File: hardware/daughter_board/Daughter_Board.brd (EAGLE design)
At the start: 65 x 30 mm, 75 parts, among them IC1 LMV358MMX, IC2 LMV358MMX, IC3 ATMEGA2560-16AU, IC4 ATMEGA16U2-MU, IC5 LMV358MMX, IC6 LP2985-33DBVR, IC7 LMV358IDGKR, IC8 LMV358MMX, IC9 LMV358MMX, J1 USB_MINI-B_SMT, T1 FDN340P, Y1 CSTCE16M0V53-R0 16MHZ, Y2 16MHz

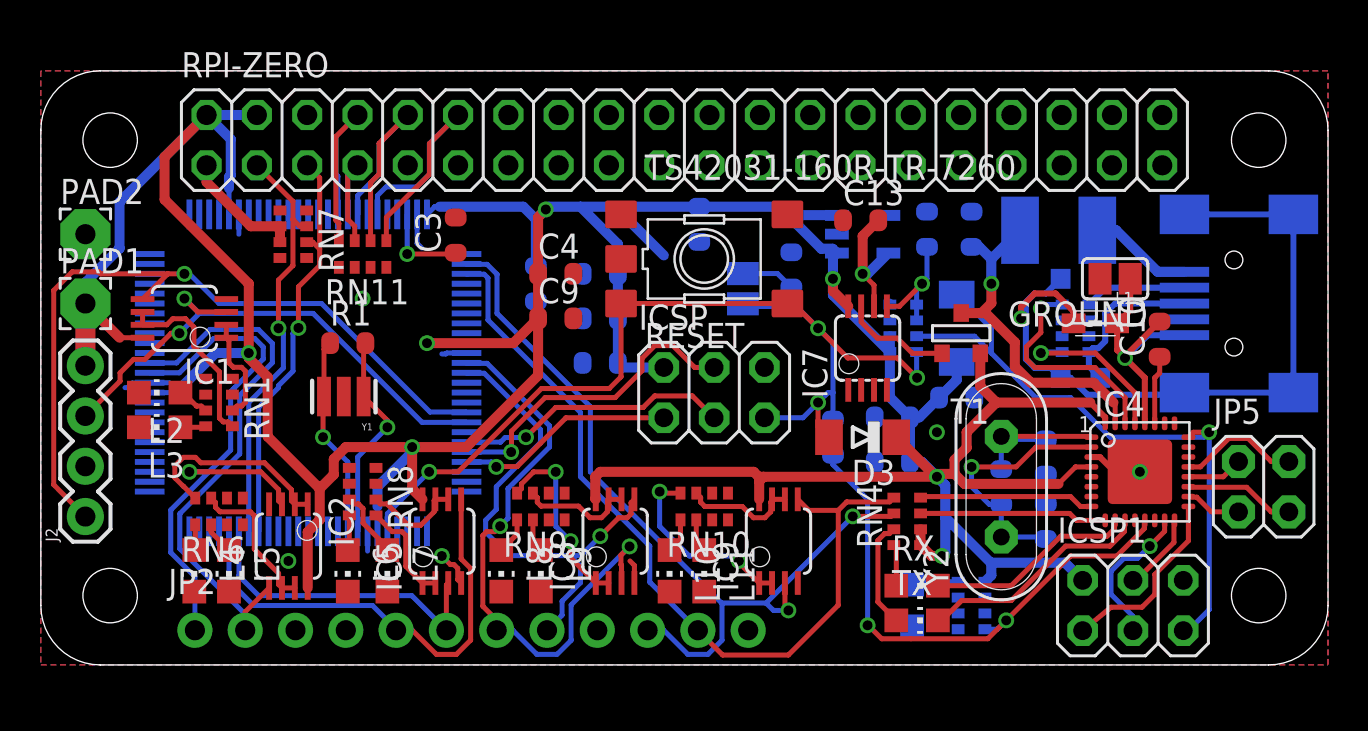
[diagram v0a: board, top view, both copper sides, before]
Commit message: partial implementation of daughter board with rpi as bootloader
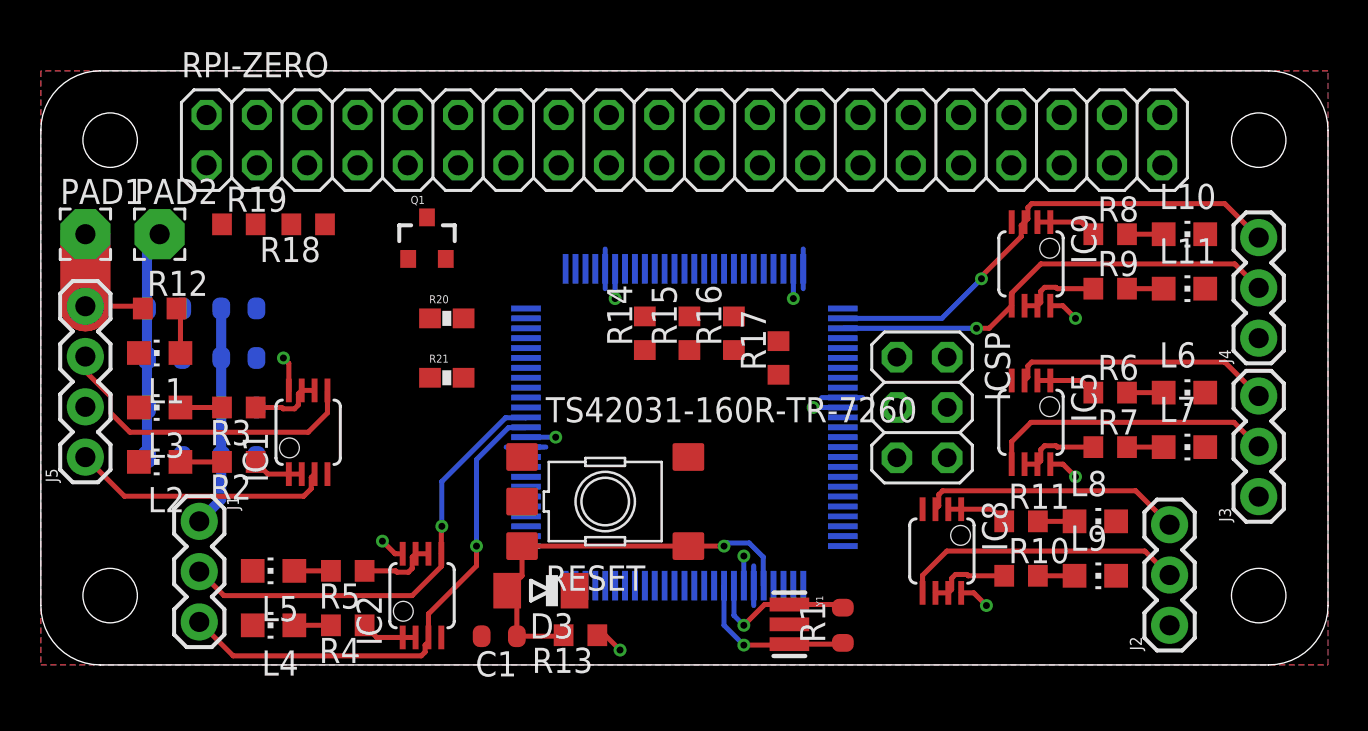
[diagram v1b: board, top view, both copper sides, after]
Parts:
- removed C10, C13: 1u, SmartPrj:C0603-ROUND
- removed C11, C12, C6, C7, C8, C9: 100n, SmartPrj:C0603-ROUND
- removed C14, C15: 22p, SmartPrj:C0603-ROUND
- removed D2: CD1206-S01575, diode:MINIMELF
- removed F1: MF-MSMF050-2 500mA, rcl:L1812
- removed GROUND, RESET-EN: (no value), jumper:SJ
- removed IC4: ATMEGA16U2-MU, SmartPrj:MLF32
- removed IC6: LP2985-33DBVR, SmartPrj:SOT23-DBV
- removed IC7: LMV358IDGKR, linear:MSOP08
- removed ICSP1: 3x2M, SmartPrj:2X03
- removed JP2: (no value), adafruit:1X12-CB
- removed JP5: 2x2M - NM, SmartPrj:2X02
- removed ON: GREEN, led:CHIP-LED0805
- removed RN1, RN10, RN11, RN3, RN4, RN6, RN8, RN9: 1k, resistor-dil:CAY16
- removed RN2: 22R, resistor-dil:CAY16
- removed RN5, RN7: 10K, resistor-dil:CAT16
- removed RX, TX: YELLOW, led:CHIP-LED0805
- removed T1: FDN340P, zetex:SOT-23
- removed Y2: 16MHz, SmartPrj:QS
- removed Z1, Z2: CG0603MLC-05E, varistor:CT/CN0603
- added J3, J4: (no value), SparkFun-Connectors:1X03
- added J5: (no value), SparkFun-Connectors:1X04
- added Q1: BSS138, SparkFun:SOT23-3
- added R10, R11, R12, R3, R4, R5, R6, R7, R8, R9: 1k, resistor:R0603
- added R13, R14, R15, R16, R17, R18, R19: 10k, resistor:R0603
- added R20, R21: 10K, SparkFun:0603-RES
- J1: value USB_MINI-B_SMT -> (none); device SparkFun-Connectors:USB-MINIB -> SparkFun-Connectors:1X03
- J2: device SparkFun-Connectors:1X04 -> SparkFun-Connectors:1X03
- L1: value BLM21 -> GREEN; device wuerth-elektronik:0805 -> led:CHIP-LED0805
- R2: value 1M -> 1k; device SmartPrj:R0603-ROUND -> resistor:R0603
- moved J2 55.0 mm to (57.0, 2.00)
- moved J1 53.4 mm to (8.00, 7.25), flipped to the top, turned to 270 degrees
- moved L1 47.3 mm to (6.00, 15.8), turned to 90 degrees
- moved L6 43.2 mm to (57.8, 13.8), turned to 270 degrees
- moved L7 40.7 mm to (57.8, 11.0), turned to 270 degrees
- moved R2 38.5 mm to (10.0, 10.2), flipped to the top, turned to 180 degrees
- moved C5 36.9 mm to (6.25, 15.5)
- moved L10 31.1 mm to (57.8, 21.8), turned to 270 degrees
- moved IC5 30.3 mm to (50.0, 12.2), turned to 180 degrees
- moved L8 30.1 mm to (53.2, 7.25), turned to 270 degrees
- moved R1 28.8 mm to (40.5, 2.00), turned to 90 degrees
- moved L11 28.1 mm to (57.8, 19.0), turned to 270 degrees
- moved L9 28.0 mm to (53.2, 4.50), turned to 270 degrees
- moved C2 26.1 mm to (10.0, 10.5), turned to 180 degrees
- moved Y1 25.3 mm to (37.8, 2.05), turned to 270 degrees
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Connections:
- removed net +3V3: C13.2, IC6.5, IC7.6
- removed net 3V3_OUT_2: RPI-ZERO.17
- removed net 8PB4: IC4.18, JP5.1
- removed net 8PB5: IC4.19, JP5.3
- removed net 8PB6: IC4.20, JP5.2
- removed net 8PB7: IC4.21, JP5.4
- removed net AREF: C3.1, IC3.98
- removed net CMP: C12.2, IC7.5, RN5.5, RN5.6
- removed net D+: J1.D+, RN2.8, Z2.2
- removed net D-: J1.D-, RN2.5, Z1.2
- removed net DTR: C7.1, IC4.13, RN3.4
- removed net GATE_CMD: IC7.7, T1.3
- removed net M8RXD: IC4.9, RN4.7
- removed net M8TXD: IC4.8, RN4.8
- removed net MISO2: IC4.17, ICSP1.1
- removed net MOSI2: IC4.16, ICSP1.4
- removed net N$54: RN4.4, RX.A
- removed net N$55: RN4.3, TX.A
- removed net PA0: IC3.78
- removed net PA1: IC3.77
- removed net PA2: IC3.76
- removed net PA3: IC3.75
- removed net PA4: IC3.74
- removed net PA5: IC3.73
- removed net PA6: IC3.72
- removed net PA7: IC3.71
- removed net PB0: IC3.19
- removed net PB4: IC3.23
- removed net PB5: IC3.24
- removed net PB6: IC3.25
- removed net PB7: IC3.26
- removed net PC0: IC3.53
- removed net PC1: IC3.54
- removed net PC2: IC3.55
- removed net PC3: IC3.56
- removed net PC4: IC3.57
- removed net PC5: IC3.58
- removed net PC6: IC3.59
- removed net PC7: IC3.60
- removed net PD7: IC3.50
- removed net PF0: IC3.97
- removed net PF1: IC3.96
- removed net PF3: IC3.94
- removed net PF7: IC3.90
- removed net PG0: IC3.51
- removed net PG1: IC3.52
- removed net PG2: IC3.70
- removed net PH3: IC3.15
- removed net PH4: IC3.16
- removed net PL0: IC3.35
- removed net PL1: IC3.36
- removed net PL2: IC3.37
- removed net PL3: IC3.38
- removed net PL4: IC3.39
- removed net PL5: IC3.40
- removed net PL6: IC3.41
- removed net PL7: IC3.42
- removed net RD+: IC4.29, RN2.1
- removed net RD-: IC4.30, RN2.4
- removed net RESET2: D2.A, IC4.24, ICSP1.5, RN5.7
- removed net RXL: IC4.10, RX.C
- removed net SCK2: IC4.15, ICSP1.3
- removed net TXL: IC4.11, TX.C
- removed net UGND: C10.2, GROUND.1, IC4.28, J1.GND, L1.1
- removed net USBVCC: C8.1, F1.1, IC4.31, T1.1
- removed net USHIELD: J1.S1, J1.S2, J1.S3, J1.S4, L1.2, Z1.1, Z2.1
- removed net VIN: RN5.3
- removed net VUCAP: C10.1, IC4.27
- removed net XT1: C14.1, IC4.1, R2.1, Y2.2
- removed net XT2: C15.1, IC4.2, R2.2, Y2.1
- removed net XVCC: F1.2, J1.VBUS
- new net HV: R21.1
- new net HV1: Q1.3, R21.2
- new net LV: Q1.1, R20.1
- new net LV1: Q1.2, R20.2
- net +5V: now also C3.1, J5.4, R12.1, R13.1; no longer C11.2, C6.1, C9.1, D2.C, IC4.32, IC4.4, IC6.1, IC6.3, IC7.8, ICSP1.2, J2.4, RN3.1, RN4.5, RN4.6, RN5.1, RN5.2, T1.2
- net 3V3_OUT: now also R14.1, R15.1, R16.1, R17.1, R18.1, R19.1, RPI-ZERO.17; no longer RN7.6, RN7.7
- net GND: now also J1.1, J2.1, J3.1, J4.1, J5.2, L1.C; no longer C11.1, C12.1, C13.1, C14.2, C15.2, C6.2, C8.2, C9.2, GROUND.2, IC4.3, IC4.33, IC6.2, IC7.4, ICSP1.6, J2.2, JP2.12, JP2.3, JP2.4, JP2.9, ON.C, RN11.1, RN11.2, RN11.3, RN11.4, RN3.5, RN5.4
- net GPIO14: now also R14.2; no longer RN11.8
- net GPIO15: now also R16.2; no longer RN11.6
- net GPIO18: now also R17.2; no longer RN11.5
- net GPIO4: now also R15.2; no longer RN11.7
- net N$1: now also R3.2; no longer RN1.8
- net N$10: now also R4.2; no longer RN6.1
- net N$11: now also R5.2; no longer RN6.2
- net N$12: now also R11.1; no longer RN9.8
- net N$13: now also R7.2; no longer RN8.7
- net N$14: now also R6.2; no longer RN8.8
- net N$15: now also R10.1; no longer RN9.7
- net N$16: now also R8.1; no longer RN10.8
- net N$17: now also R9.1; no longer RN10.7
- net N$18: now also R9.2; no longer RN10.2
- net N$19: now also R8.2; no longer RN10.1
- net N$2: now also R2.2; no longer RN1.7
- net N$21: now also R11.2; no longer RN9.1
- net N$22: now also R10.2; no longer RN9.2
- net N$3: now also L1.A, R12.2; no longer ON.A, RN3.8
- net N$4: now also R2.1; no longer RN1.2
- net N$5: now also R7.1; no longer RN8.2
- net N$6: now also R3.1; no longer RN1.1
- net N$7: now also R6.1; no longer RN8.1
- net N$8: now also R5.1; no longer RN6.7
- net N$9: now also R4.1; no longer RN6.8
- net PE0: now also J4.3; no longer JP2.10, RN4.2
- net PE1: now also J4.2; no longer JP2.11, RN4.1
- net PH5: now also IC1.3, J5.1; no longer IC1.5, J2.1
- net PH6: now also IC1.5, J5.3; no longer IC1.3, J2.3
- net RESET: now also R13.2; no longer C7.2, RESET-EN.1, RESET-EN.2, RN5.8
- net RXD1: now also J3.3; no longer JP2.6
- net RXD2: now also J2.3; no longer JP2.7
- net RXD3: now also J1.3; no longer JP2.1
- net SCL: now also R18.2; no longer IC3.43, RN7.2
- net SDA: now also R19.2; no longer IC3.44, RN7.3
- net TXD1: now also J3.2; no longer JP2.5
- net TXD2: now also J2.2; no longer JP2.8
- net TXD3: now also J1.2; no longer JP2.2
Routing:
- net +5V: track 221.8 -> 25.8 mm, vias 7 -> 6
- net USHIELD: track 39.2 -> 0.00 mm, vias 1 -> 0
- net RESET: track 56.3 -> 21.4 mm, vias 4 -> 1
- net RESET2: track 32.6 -> 0.00 mm, vias 1 -> 0
- net DTR: track 27.6 -> 0.00 mm, vias 2 -> 0
- net PH5: track 38.1 -> 13.2 mm, vias 1 -> 0
- net SDA: track 21.2 -> 0.00 mm, vias 1 -> 0
- net SCL: track 20.8 -> 0.00 mm, vias 1 -> 0
- net PE1: track 42.1 -> 23.2 mm, vias 0 -> 1
- net PE0: track 42.8 -> 24.8 mm, vias 2 -> 1
- net USBVCC: track 17.6 -> 0.00 mm, vias 1 -> 0
- net RXD2: track 30.3 -> 13.3 mm, vias 2 -> 0
- net GND: track 13.6 -> 30.2 mm
- net PB2: track 16.2 -> 0.00 mm, vias 1 -> 0
- net GPIO18: track 15.5 -> 0.00 mm
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- added copper zone on layer 16, net +5V
- removed copper zone on layer 16, net GND

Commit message: route icsp header
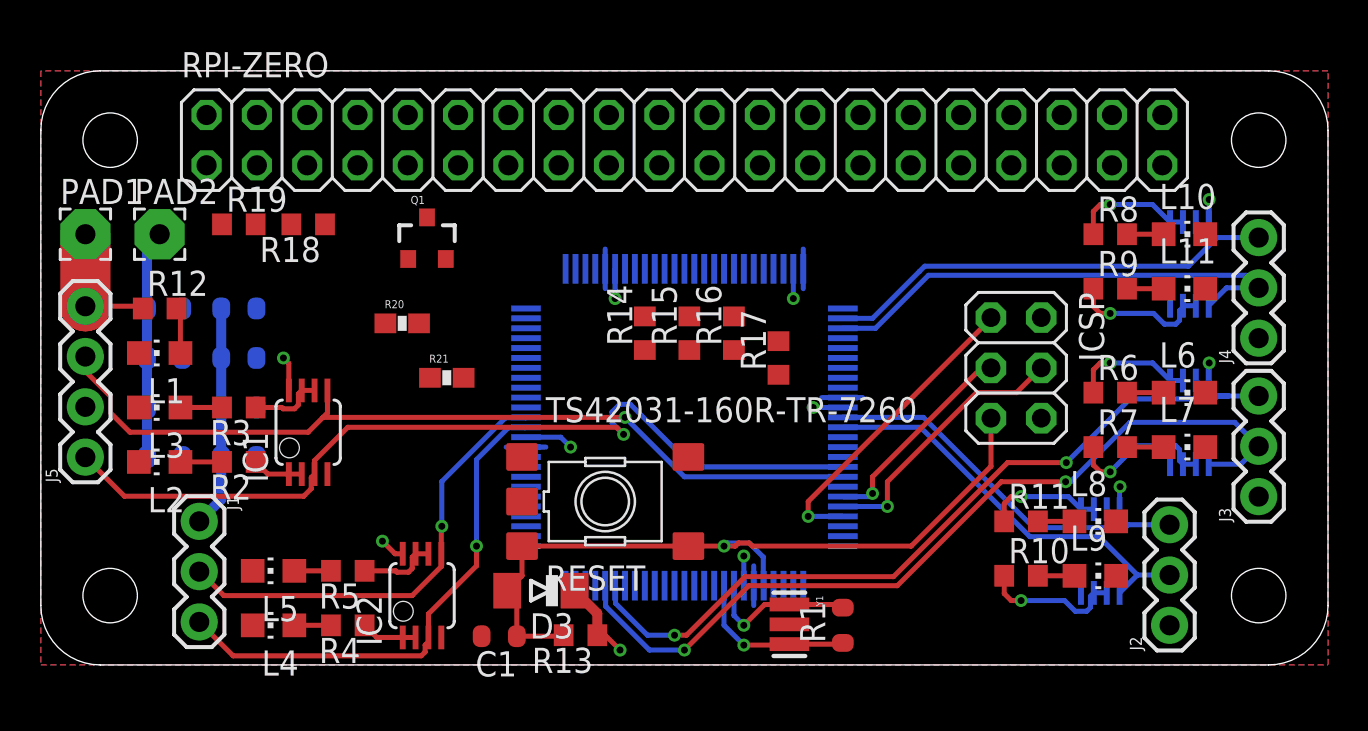
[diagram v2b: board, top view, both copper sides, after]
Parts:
- moved IC5 8.00 mm to (58.0, 12.2), flipped to the bottom
- moved IC8 8.00 mm to (53.5, 5.75), flipped to the bottom
- moved IC9 8.00 mm to (58.0, 20.2), flipped to the bottom
- moved ICSP 5.15 mm to (49.2, 15.0)
- moved R20 2.26 mm to (18.2, 17.2)
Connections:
- net SCL: now also IC3.43
- net SDA: now also IC3.44
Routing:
- net PH5: track 13.2 -> 44.8 mm, vias 0 -> 1
- net TXD1: track 14.5 -> 43.1 mm, vias 0 -> 2
- net RXD1: track 13.3 -> 41.5 mm, vias 0 -> 2
- net PH6: track 16.3 -> 43.8 mm, vias 0 -> 1
- net RESET: track 21.4 -> 39.2 mm
- net PB3: track 0.00 -> 15.6 mm, vias 0 -> 1
- net PB2: track 0.00 -> 13.7 mm, vias 0 -> 1
- net PB1: track 0.00 -> 10.7 mm, vias 0 -> 1
- net RXD2: track 13.3 -> 19.9 mm
- net TXD2: track 14.4 -> 20.9 mm
- net GND: track 30.2 -> 34.4 mm, vias 5 -> 8
- net N$5: track 4.22 -> 7.48 mm, vias 0 -> 1
- net N$7: track 3.08 -> 6.19 mm, vias 0 -> 1
- net N$16: track 3.08 -> 6.19 mm, vias 0 -> 1
- net N$17: track 4.22 -> 7.19 mm, vias 0 -> 1
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
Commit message: level converter and labels
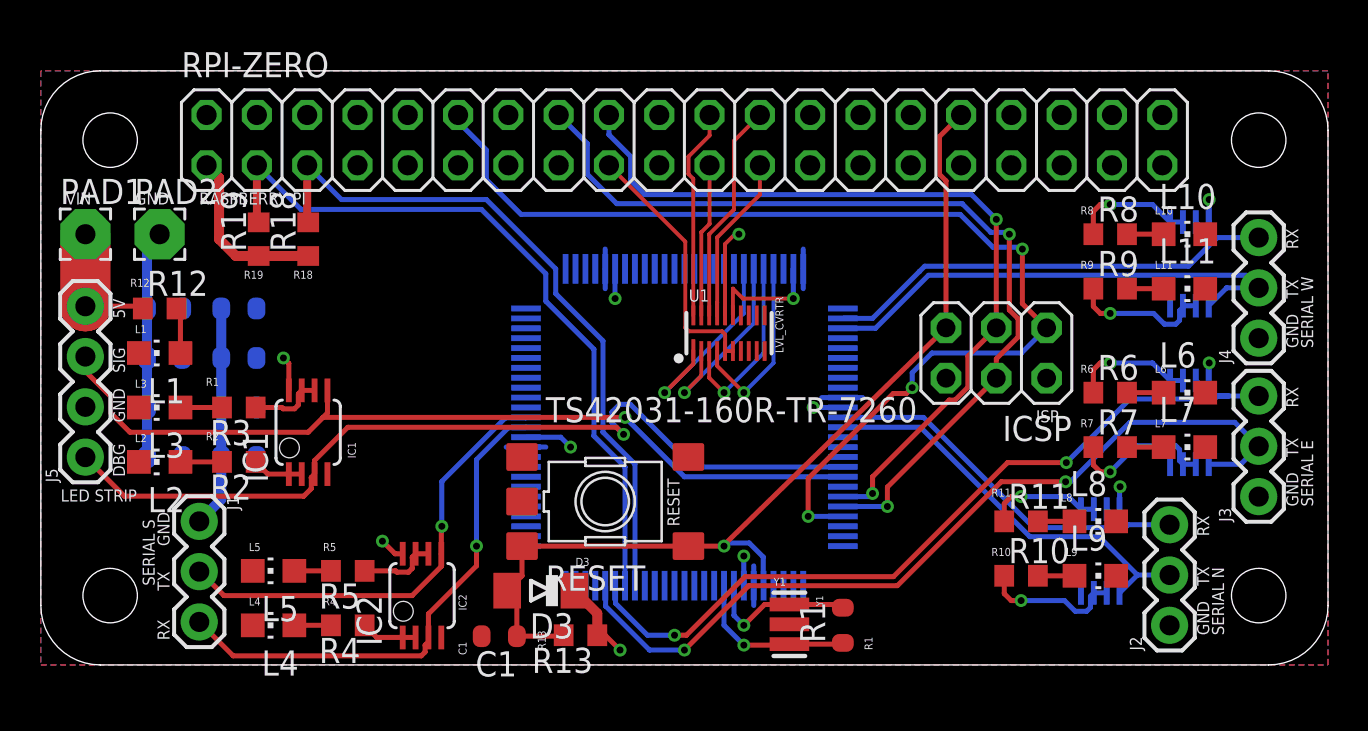
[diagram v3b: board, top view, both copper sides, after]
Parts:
- removed Q1: BSS138, SparkFun:SOT23-3
- removed R14, R15, R16, R17: 10k, resistor:R0603
- removed R20, R21: 10K, SparkFun:0603-RES
- added U1: TXB0108DQSR, SparkFun-IC-Comms:UFDFN-20
- moved ICSP 1.25 mm to (48.2, 15.8), turned to 180 degrees
- moved R19 1.25 mm to (11.0, 21.5), turned to 90 degrees
- moved R18 0.75 mm to (13.5, 21.5), turned to 90 degrees
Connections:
- removed net GPIO12: RPI-ZERO.32
- removed net GPIO18: IC3.95, R17.2, RPI-ZERO.12
- removed net GPIO23: RPI-ZERO.16
- removed net GPIO24: RPI-ZERO.18
- removed net HV: R21.1
- removed net HV1: Q1.3, R21.2
- removed net LV: Q1.1, R20.1
- removed net LV1: Q1.2, R20.2
- new net ARDU_0: IC3.97, U1.4
- new net ARDU_1: IC3.96, U1.3
- new net ARDU_2: IC3.95, U1.2
- new net ARDU_3: IC3.94, U1.1
- net +5V: now also U1.16
- net 3V3_OUT: now also U1.5, U1.6; no longer R14.1, R15.1, R16.1, R17.1
- net GND: now also U1.15
- net GPIO11: now also U1.17
- net GPIO14: no longer IC3.91, R14.2
- net GPIO15: no longer IC3.93, R16.2
- net GPIO25: now also U1.20
- net GPIO4: no longer IC3.92, R15.2
- net GPIO8: now also U1.18
- net GPIO9: now also U1.19
- net PB1: now also RPI-ZERO.18
- net PB2: now also RPI-ZERO.16
- net PB3: now also RPI-ZERO.12
- net RESET: now also RPI-ZERO.32
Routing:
- net PB3: track 15.6 -> 56.2 mm, vias 1 -> 3
- net SDA: track 0.00 -> 37.2 mm
- net SCL: track 0.00 -> 35.3 mm
- net PB2: track 13.7 -> 45.1 mm, vias 1 -> 2
- net PB1: track 10.7 -> 41.2 mm, vias 1 -> 2
- net 3V3_OUT: track 0.00 -> 22.0 mm
- net GPIO8: track 0.00 -> 11.2 mm
- net GPIO25: track 0.00 -> 10.7 mm
- net ARDU_3: track 0.00 -> 10.7 mm, vias 0 -> 1
- net ARDU_2: track 0.00 -> 10.2 mm, vias 0 -> 1
- net ARDU_0: track 0.00 -> 9.53 mm, vias 0 -> 1
- net ARDU_1: track 0.00 -> 9.49 mm, vias 0 -> 1
- net RESET: track 39.2 -> 48.5 mm
- net GPIO11: track 0.00 -> 8.47 mm
- net GPIO9: track 0.00 -> 7.75 mm
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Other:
- board text added: "5V"
- board text added: "C1"
- board text added: "C16"
- board text added: "C17"
- board text added: "C19"
- board text added: "C2"
- board text added: "C3"
- board text added: "C4"
- board text added: "C5"
- board text added: "D3"
- board text added: "DBG"
- board text added: "GND"
- board text added: "IC1"
- board text added: "IC2"
- board text added: "IC5"
- board text added: "IC8"
- board text added: "IC9"
- board text added: "ISP"
- board text added: "L1"
- board text added: "L10"
- board text added: "L11"
- board text added: "L2"
- board text added: "L3"
- board text added: "L4"
- board text added: "L5"
- board text added: "L6"
- board text added: "L7"
- board text added: "L8"
- board text added: "L9"
- board text added: "LED STRIP"
- board text added: "LVL_CVRTR"
- board text added: "R1"
- board text added: "R10"
- board text added: "R11"
- board text added: "R12"
- board text added: "R13"
- board text added: "R18"
- board text added: "R19"
- board text added: "R2"
- board text added: "R4"
- board text added: "R5"
- board text added: "R6"
- board text added: "R7"
- board text added: "R8"
- board text added: "R9"
- board text added: "RASPBERRY PI"
- board text added: "RESET"
- board text added: "RX"
- board text added: "SERIAL E"
- board text added: "SERIAL N"
- board text added: "SERIAL S"
- board text added: "SERIAL W"
- board text added: "SIG"
- board text added: "TX"
- board text added: "VIN"
- board text added: "Y1"
